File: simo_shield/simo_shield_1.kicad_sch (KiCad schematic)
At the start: 6 parts, among them J1 modulo_usb_debug, J2 conector_bateria, U1 elemon_board, U2 modulo_flash_externa, U3 bluepill_board_stm32, U4 modulo_acelerometro

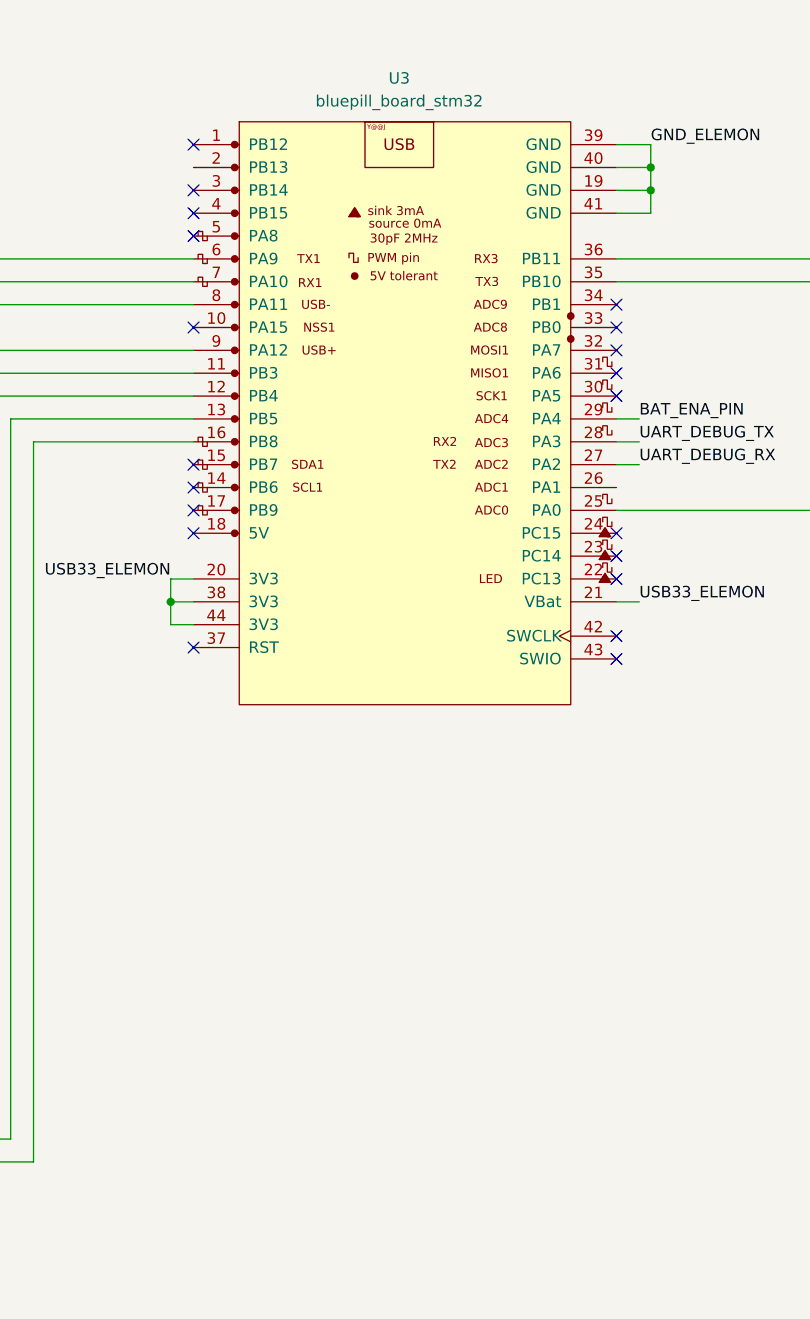
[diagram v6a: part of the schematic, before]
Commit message: simo_shield: Listo para primera revision de pcb
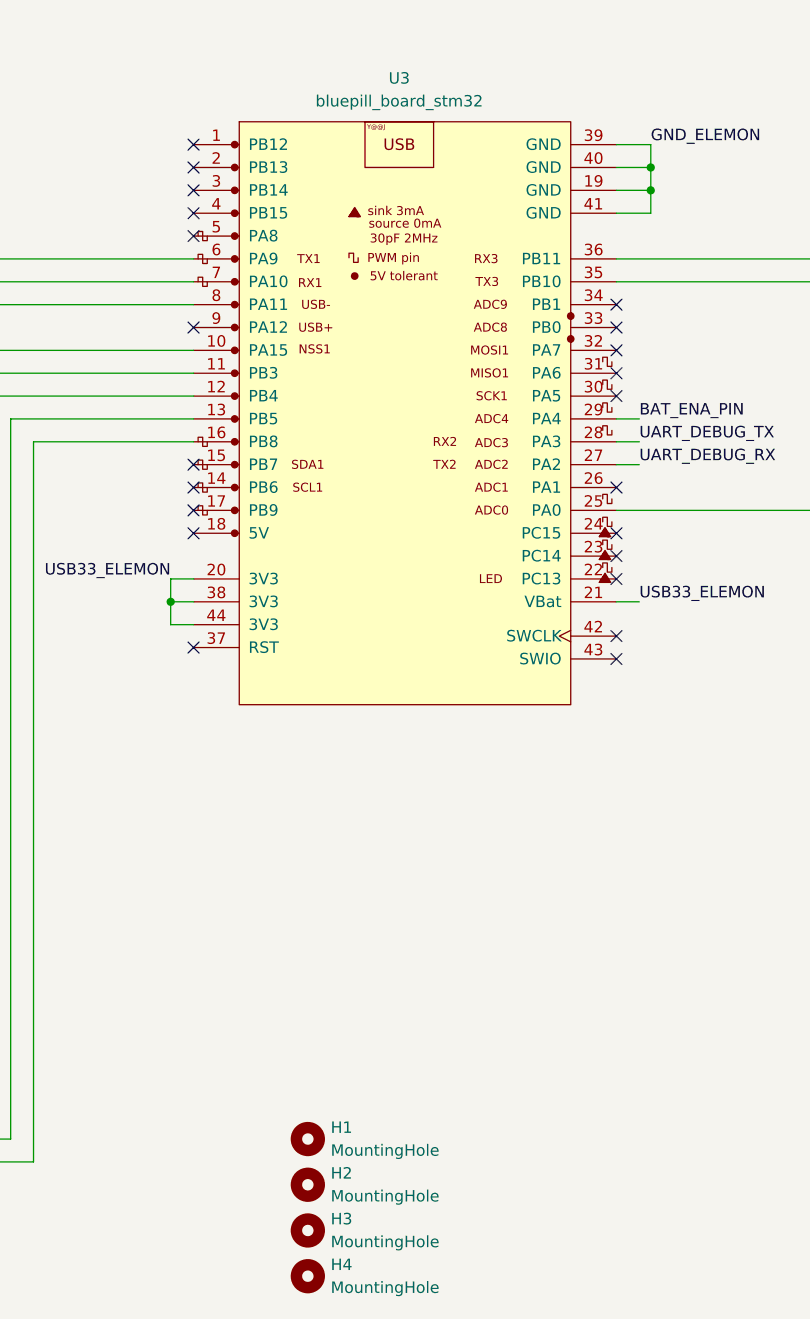
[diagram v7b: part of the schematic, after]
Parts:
- added H1, H2, H3, H4: MountingHole, simo_shield:MountingHole_3mm, symbol simo_shield:MountingHole
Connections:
- net at U1.14 (RI): now also U3.10 (PA15); no longer U3.9 (PA12)
- no-connect marks 74 -> 76
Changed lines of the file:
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@@
   (junction (at 124.46 110.49) (diameter 0) (color 0 0 0 0)
   )
+  (no_connect (at 127 62.23))
   (no_connect (at 127 69.85))
   (no_connect (at 127 80.01))
@@
   (no_connect (at 173.99 80.01))
   (no_connect (at 173.99 114.3))
+  (no_connect (at 173.99 97.79))
   (no_connect (at 34.29 66.04))
   (no_connect (at 34.29 63.5))
@@
   (label "GND_ELEMON" (at 177.8 59.69 0)
     (effects (font (size 1.27 1.27)) (justify left bottom))
+  )
+  (symbol (lib_id "simo_shield:MountingHole") (at 139.7 170.18 0) (unit 1)
+    (in_bom yes) (on_board yes) (fields_autoplaced)
+    (property "Reference" "H1" (id 0) (at 142.24 168.9099 0)
+      (effects (font (size 1.27 1.27)) (justify left))
+    )
+    (property "Value" "MountingHole" (id 1) (at 142.24 171.4499 0)
+      (effects (font (size 1.27 1.27)) (justify left))
+    )
+    (property "Footprint" "simo_shield:MountingHole_3mm" (id 2) (at 139.7 170.18 0)
+      (effects (font (size 1.27 1.27)) hide)
+    )
+    (property "Datasheet" "~" (id 3) (at 139.7 170.18 0)
+      (effects (font (size 1.27 1.27)) hide)
+    )
+  )
+  (symbol (lib_id "simo_shield:MountingHole") (at 139.7 185.42 0) (unit 1)
+    (in_bom yes) (on_board yes) (fields_autoplaced)
+    (property "Reference" "H4" (id 0) (at 142.24 184.1499 0)
+      (effects (font (size 1.27 1.27)) (justify left))
+    )
+    (property "Value" "MountingHole" (id 1) (at 142.24 186.6899 0)
+      (effects (font (size 1.27 1.27)) (justify left))
+    )
+    (property "Footprint" "simo_shield:MountingHole_3mm" (id 2) (at 139.7 185.42 0)
+      (effects (font (size 1.27 1.27)) hide)
+    )
+    (property "Datasheet" "~" (id 3) (at 139.7 185.42 0)
+      (effects (font (size 1.27 1.27)) hide)
+    )
   )
   (symbol (lib_id "simo_shield:modulo_flash_externa") (at 52.07 157.48 0) (mirror y) (unit 1)
@@
     (pin "56")
   )
+  (symbol (lib_id "simo_shield:MountingHole") (at 139.7 175.26 0) (unit 1)
+    (in_bom yes) (on_board yes) (fields_autoplaced)
+    (property "Reference" "H2" (id 0) (at 142.24 173.9899 0)
+      (effects (font (size 1.27 1.27)) (justify left))
+    )
+    (property "Value" "MountingHole" (id 1) (at 142.24 176.5299 0)
+      (effects (font (size 1.27 1.27)) (justify left))
+    )
+    (property "Footprint" "simo_shield:MountingHole_3mm" (id 2) (at 139.7 175.26 0)
+      (effects (font (size 1.27 1.27)) hide)
+    )
+    (property "Datasheet" "~" (id 3) (at 139.7 175.26 0)
+      (effects (font (size 1.27 1.27)) hide)
+    )
+  )
+  (symbol (lib_id "simo_shield:MountingHole") (at 139.7 180.34 0) (unit 1)
+    (in_bom yes) (on_board yes) (fields_autoplaced)
+    (property "Reference" "H3" (id 0) (at 142.24 179.0699 0)
+      (effects (font (size 1.27 1.27)) (justify left))
+    )
+    (property "Value" "MountingHole" (id 1) (at 142.24 181.6099 0)
+      (effects (font (size 1.27 1.27)) (justify left))
+    )
+    (property "Footprint" "simo_shield:MountingHole_3mm" (id 2) (at 139.7 180.34 0)
+      (effects (font (size 1.27 1.27)) hide)
+    )
+    (property "Datasheet" "~" (id 3) (at 139.7 180.34 0)
+      (effects (font (size 1.27 1.27)) hide)
+    )
+  )
   (symbol (lib_name "modulo_usb_debug_1") (lib_id "simo_shield:modulo_usb_debug") (at 238.76 129.54 0) (unit 1)
     (in_bom yes) (on_board yes) (fields_autoplaced)
@@
   )
   (symbol_instances
+    (path "/018656e2-ef90-4c97-a0c5-e8db386dca1e"
+      (reference "H1") (unit 1) (value "MountingHole") (footprint "simo_shield:MountingHole_3mm")
+    )
+    (path "/e7311ad4-372c-4939-9b74-10c612a07e06"
+      (reference "H2") (unit 1) (value "MountingHole") (footprint "simo_shield:MountingHole_3mm")
+    )
+    (path "/f0275c00-99ab-4712-b483-b261a0f3c72e"
+      (reference "H3") (unit 1) (value "MountingHole") (footprint "simo_shield:MountingHole_3mm")
+    )
+    (path "/1ad3c611-8dd1-4ae5-8bec-8d19dfb9183c"
+      (reference "H4") (unit 1) (value "MountingHole") (footprint "simo_shield:MountingHole_3mm")
+    )
     (path "/fc6149f3-6c8e-44e2-b6f1-cd1c7ffb6984"
       (reference "J1") (unit 1) (value "modulo_usb_debug") (footprint "simo_shield:JST_EH_B2B-EH-A_1x02_P2.50mm_Vertical")

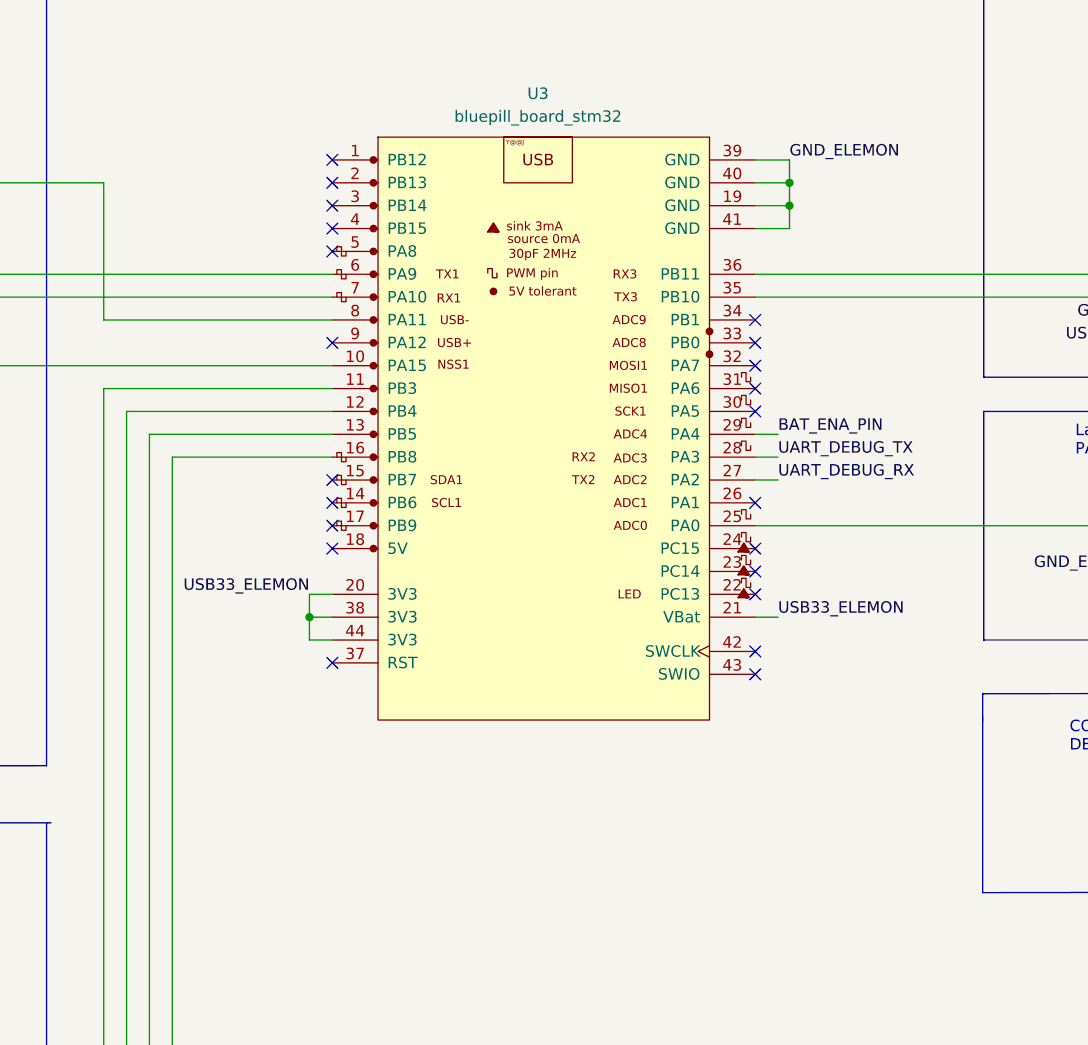
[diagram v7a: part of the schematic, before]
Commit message: actualizacion en placa simo shield: correccion de inconsistencias en el modulo bluepill clone
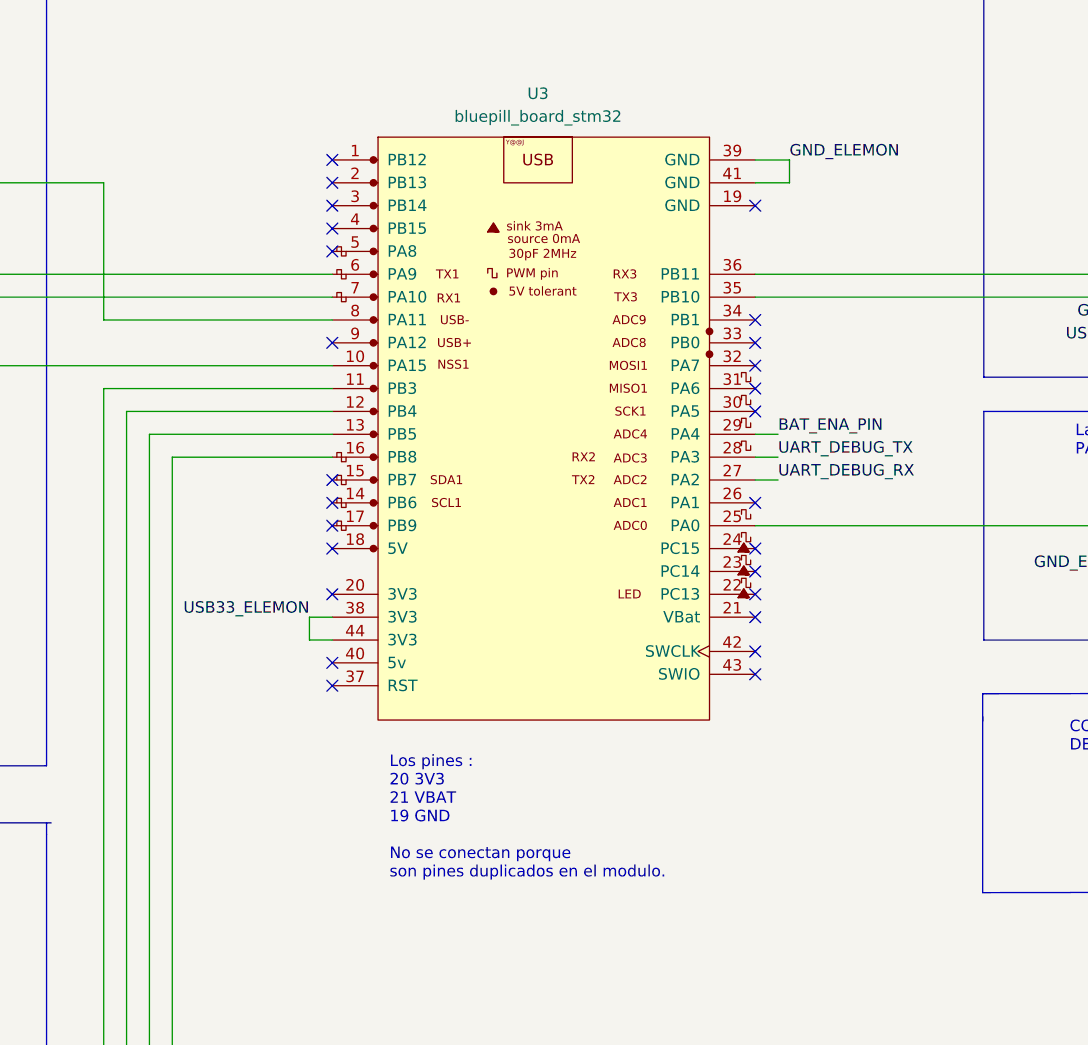
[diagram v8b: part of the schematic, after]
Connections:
- net GND_ELEMON: no longer U3.19 (GND), U3.40 (GND)
- net USB33_ELEMON: no longer U3.20 (3V3), U3.21 (VBat)
- no-connect marks 76 -> 80
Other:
- note added: "Los pines : 20 3V3 21 VBAT 19 GND No se conectan porque son pines duplicados en el modulo."
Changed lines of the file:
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@@
     (comment 5 "Descripcion:")
   )
-  (junction (at 177.8 62.23) (diameter 0) (color 0 0 0 0)
-  )
-  (junction (at 177.8 64.77) (diameter 0) (color 0 0 0 0)
-  )
-  (junction (at 124.46 110.49) (diameter 0) (color 0 0 0 0)
-  )
+  (no_connect (at 127 118.11))
   (no_connect (at 127 62.23))
   (no_connect (at 127 69.85))
@@
   (no_connect (at 173.99 102.87))
   (no_connect (at 173.99 105.41))
+  (no_connect (at 173.99 110.49))
   (no_connect (at 67.31 105.41))
   (no_connect (at 223.52 62.23))
@@
   (no_connect (at 173.99 80.01))
   (no_connect (at 173.99 114.3))
+  (no_connect (at 127 107.95))
   (no_connect (at 173.99 97.79))
   (no_connect (at 34.29 66.04))
@@
   (no_connect (at 34.29 87.63))
   (no_connect (at 173.99 82.55))
+  (no_connect (at 173.99 64.77))
   (no_connect (at 67.31 118.11))
   (no_connect (at 67.31 115.57))
@@
   (no_connect (at 173.99 116.84))
   (no_connect (at 127 115.57))
-  (wire (pts (xy 173.99 110.49) (xy 176.53 110.49))
-    (stroke (width 0) (type default) (color 0 0 0 0))
-  )
   (wire (pts (xy 54.61 167.64) (xy 104.14 167.64))
     (stroke (width 0) (type default) (color 0 0 0 0))
   )
-  (wire (pts (xy 177.8 62.23) (xy 177.8 64.77))
+  (wire (pts (xy 177.8 59.69) (xy 177.8 62.23))
     (stroke (width 0) (type default) (color 0 0 0 0))
   )
@@
     (stroke (width 0) (type default) (color 0 0 0 0))
   )
-  (wire (pts (xy 177.8 59.69) (xy 177.8 62.23))
-    (stroke (width 0) (type default) (color 0 0 0 0))
-  )
   (wire (pts (xy 173.99 92.71) (xy 176.53 92.71))
     (stroke (width 0) (type default) (color 0 0 0 0))
@@
     (stroke (width 0) (type default) (color 0 0 0 0))
   )
+  (polyline (pts (xy 199.263 141.097) (xy 199.263 121.539))
+    (stroke (width 0) (type default) (color 0 0 0 0))
+  )
+  (polyline (pts (xy 13.843 127.127) (xy 13.843 15.875))
+    (stroke (width 0) (type default) (color 0 0 0 0))
+  )
+  (polyline (pts (xy 13.589 188.214) (xy 13.97 134.112))
+    (stroke (width 0) (type default) (color 0 0 0 0))
+  )
+  (wire (pts (xy 30.48 107.95) (xy 34.29 107.95))
+    (stroke (width 0) (type default) (color 0 0 0 0))
+  )
+  (wire (pts (xy 54.61 172.72) (xy 109.22 172.72))
+    (stroke (width 0) (type default) (color 0 0 0 0))
+  )
+  (polyline (pts (xy 199.644 118.999) (xy 282.956 118.872))
+    (stroke (width 0) (type default) (color 0 0 0 0))
+  )
+  (wire (pts (xy 106.68 90.17) (xy 106.68 170.18))
+    (stroke (width 0) (type default) (color 0 0 0 0))
+  )
+  (polyline (pts (xy 283.21 87.63) (xy 283.21 113.03))
+    (stroke (width 0) (type default) (color 0 0 0 0))
+  )
+  (wire (pts (xy 109.22 92.71) (xy 127 92.71))
+    (stroke (width 0) (type default) (color 0 0 0 0))
+  )
+  (polyline (pts (xy 199.263 118.999) (xy 199.644 118.999))
+    (stroke (width 0) (type default) (color 0 0 0 0))
+  )
+  (polyline (pts (xy 17.78 15.875) (xy 95.25 15.748))
+    (stroke (width 0) (type default) (color 0 0 0 0))
+  )
+  (polyline (pts (xy 283.21 140.97) (xy 199.263 141.097))
+    (stroke (width 0) (type default) (color 0 0 0 0))
+  )
+  (polyline (pts (xy 283.21 113.03) (xy 199.39 113.03))
+    (stroke (width 0) (type default) (color 0 0 0 0))
+  )
+  (polyline (pts (xy 95.25 134.62) (xy 95.25 187.071))
+    (stroke (width 0) (type default) (color 0 0 0 0))
+  )
+  (wire (pts (xy 101.6 85.09) (xy 127 85.09))
+    (stroke (width 0) (type default) (color 0 0 0 0))
+  )
+  (polyline (pts (xy 13.843 15.875) (xy 17.78 15.875))
+    (stroke (width 0) (type default) (color 0 0 0 0))
+  )
+  (wire (pts (xy 104.14 167.64) (xy 104.14 87.63))
+    (stroke (width 0) (type default) (color 0 0 0 0))
+  )
+  (wire (pts (xy 67.31 113.03) (xy 69.85 113.03))
+    (stroke (width 0) (type default) (color 0 0 0 0))
+  )
   (wire (pts (xy 173.99 62.23) (xy 177.8 62.23))
     (stroke (width 0) (type default) (color 0 0 0 0))
   )
-  (polyline (pts (xy 199.263 141.097) (xy 199.263 121.539))
-    (stroke (width 0) (type default) (color 0 0 0 0))
-  )
-  (polyline (pts (xy 13.843 127.127) (xy 13.843 15.875))
-    (stroke (width 0) (type default) (color 0 0 0 0))
-  )
-  (polyline (pts (xy 13.589 188.214) (xy 13.97 134.112))
-    (stroke (width 0) (type default) (color 0 0 0 0))
-  )
-  (wire (pts (xy 30.48 107.95) (xy 34.29 107.95))
-    (stroke (width 0) (type default) (color 0 0 0 0))
-  )
-  (wire (pts (xy 54.61 172.72) (xy 109.22 172.72))
-    (stroke (width 0) (type default) (color 0 0 0 0))
-  )
-  (polyline (pts (xy 199.644 118.999) (xy 282.956 118.872))
-    (stroke (width 0) (type default) (color 0 0 0 0))
-  )
-  (wire (pts (xy 106.68 90.17) (xy 106.68 170.18))
-    (stroke (width 0) (type default) (color 0 0 0 0))
-  )
-  (polyline (pts (xy 283.21 87.63) (xy 283.21 113.03))
-    (stroke (width 0) (type default) (color 0 0 0 0))
-  )
-  (wire (pts (xy 109.22 92.71) (xy 127 92.71))
-    (stroke (width 0) (type default) (color 0 0 0 0))
-  )
-  (polyline (pts (xy 199.263 118.999) (xy 199.644 118.999))
-    (stroke (width 0) (type default) (color 0 0 0 0))
-  )
-  (wire (pts (xy 124.46 107.95) (xy 127 107.95))
-    (stroke (width 0) (type default) (color 0 0 0 0))
-  )
-  (polyline (pts (xy 17.78 15.875) (xy 95.25 15.748))
-    (stroke (width 0) (type default) (color 0 0 0 0))
-  )
-  (polyline (pts (xy 283.21 140.97) (xy 199.263 141.097))
-    (stroke (width 0) (type default) (color 0 0 0 0))
-  )
-  (polyline (pts (xy 283.21 113.03) (xy 199.39 113.03))
-    (stroke (width 0) (type default) (color 0 0 0 0))
-  )
-  (polyline (pts (xy 95.25 134.62) (xy 95.25 187.071))
-    (stroke (width 0) (type default) (color 0 0 0 0))
-  )
-  (wire (pts (xy 101.6 85.09) (xy 127 85.09))
-    (stroke (width 0) (type default) (color 0 0 0 0))
-  )
-  (polyline (pts (xy 13.843 15.875) (xy 17.78 15.875))
-    (stroke (width 0) (type default) (color 0 0 0 0))
-  )
-  (wire (pts (xy 104.14 167.64) (xy 104.14 87.63))
-    (stroke (width 0) (type default) (color 0 0 0 0))
-  )
-  (wire (pts (xy 67.31 113.03) (xy 69.85 113.03))
-    (stroke (width 0) (type default) (color 0 0 0 0))
-  )
-  (wire (pts (xy 173.99 64.77) (xy 177.8 64.77))
-    (stroke (width 0) (type default) (color 0 0 0 0))
-  )
   (polyline (pts (xy 283.21 40.64) (xy 283.21 83.82))
     (stroke (width 0) (type default) (color 0 0 0 0))
@@
     (stroke (width 0) (type default) (color 0 0 0 0))
   )
-  (wire (pts (xy 177.8 67.31) (xy 177.8 64.77))
-    (stroke (width 0) (type default) (color 0 0 0 0))
-  )
   (wire (pts (xy 101.6 85.09) (xy 101.6 165.1))
     (stroke (width 0) (type default) (color 0 0 0 0))
@@
     (stroke (width 0) (type default) (color 0 0 0 0))
   )
-  (wire (pts (xy 124.46 107.95) (xy 124.46 110.49))
-    (stroke (width 0) (type default) (color 0 0 0 0))
-  )
   (wire (pts (xy 67.31 62.23) (xy 101.6 62.23))
     (stroke (width 0) (type default) (color 0 0 0 0))
@@
     (stroke (width 0) (type default) (color 0 0 0 0))
   )
-  (wire (pts (xy 173.99 67.31) (xy 177.8 67.31))
-    (stroke (width 0) (type default) (color 0 0 0 0))
-  )
   (wire (pts (xy 54.61 162.56) (xy 63.5 162.56))
     (stroke (width 0) (type default) (color 0 0 0 0))
   )
   (text "CONECTOR DE SALIDA \nDEL UART_DEBUG DEL PROGRAMA" (at 208.915 125.603 0)
+    (effects (font (size 1.27 1.27)) (justify left bottom))
+  )
+  (text "Los pines :\n20 3V3\n21 VBAT\n19 GND\n\nNo se conectan porque \nson pines duplicados en el modulo."
+    (at 133.35 139.7 0)
     (effects (font (size 1.27 1.27)) (justify left bottom))
   )
@@
     (effects (font (size 1.27 1.27)) (justify left bottom))
   )
-  (label "USB33_ELEMON" (at 124.46 107.95 180)
+  (label "USB33_ELEMON" (at 124.46 110.49 180)
     (effects (font (size 1.27 1.27)) (justify right bottom))
   )
@@
     (effects (font (size 1.27 1.27)) (justify left bottom))
   )
-  (label "USB33_ELEMON" (at 176.53 110.49 0)
-    (effects (font (size 1.27 1.27)) (justify left bottom))
-  )
